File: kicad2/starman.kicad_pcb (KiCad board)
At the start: 2 copper layers, 160 x 150 mm, 156 parts, among them J1 Barrel_Jack, P1 USB_C_Plug_USB2.0, U1 ESP32-S2-MINI-1, U2 PCA9959, U3 PCA9959, U4 PCA9959, U5 PCA9959, U6 LF33_TO220, U7 LF50_TO220, U8 PCA9959, U9 PCA9959

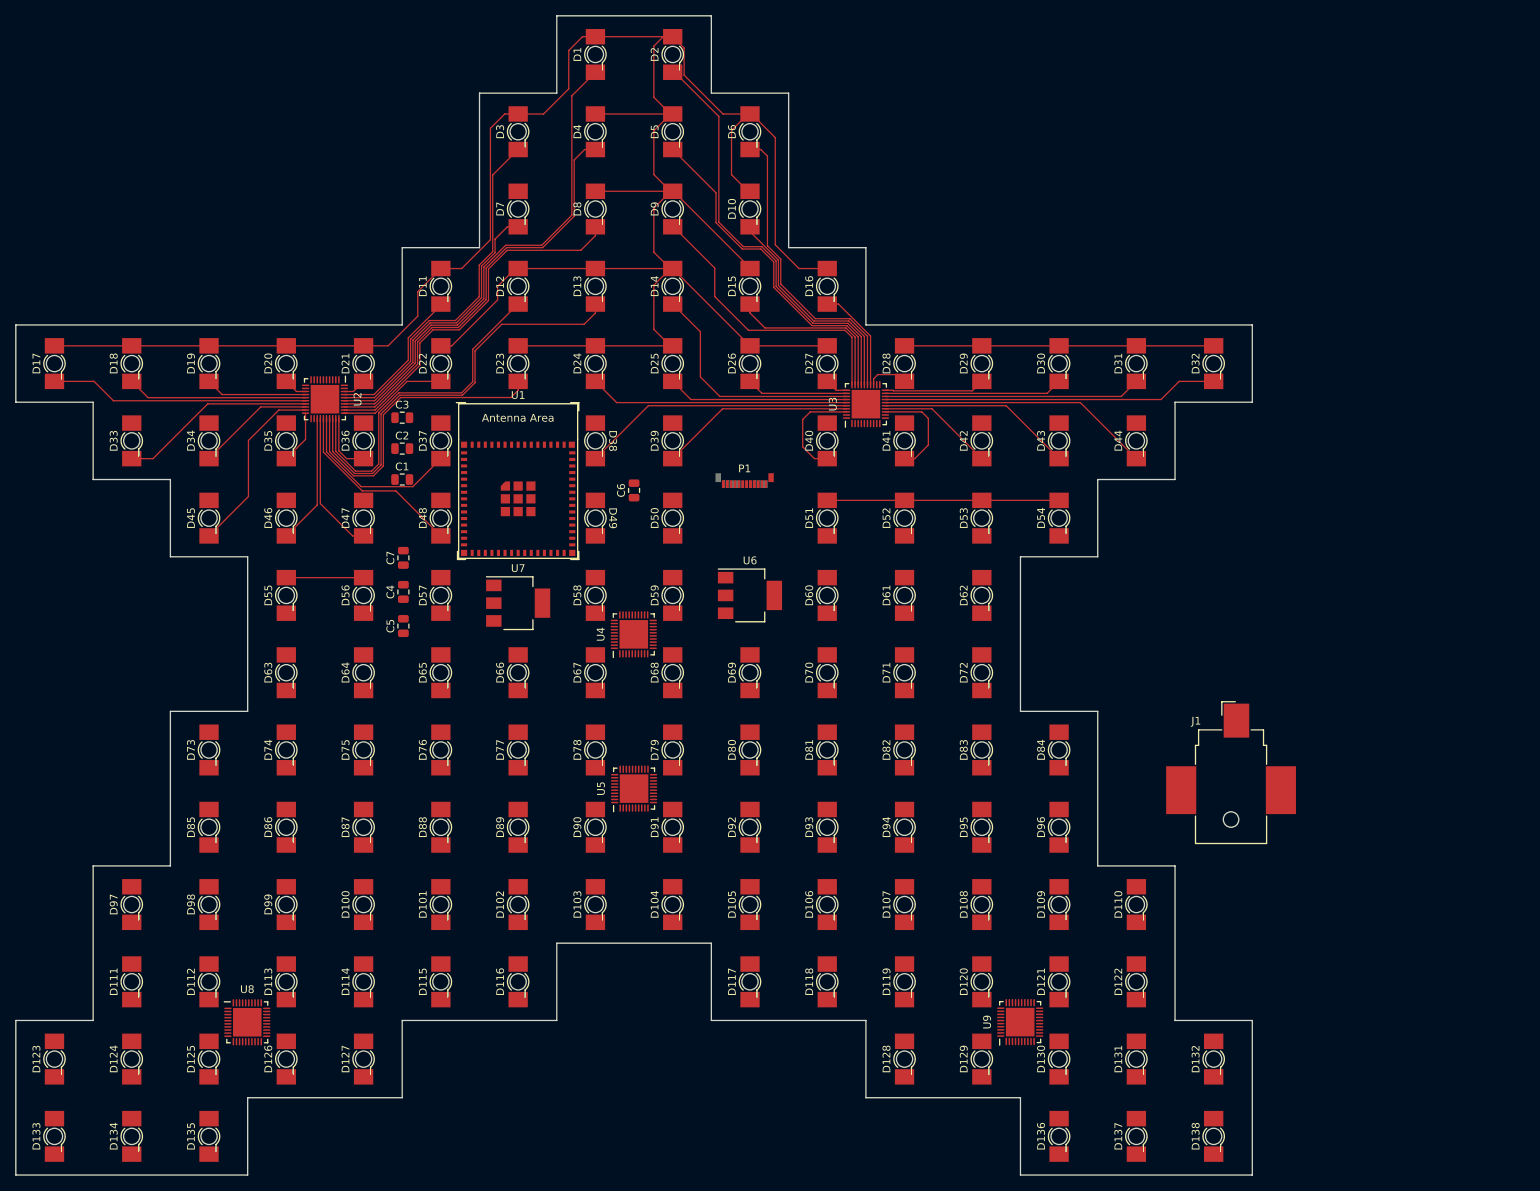
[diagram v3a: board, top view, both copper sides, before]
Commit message: Completed tracks to and from LED drivers
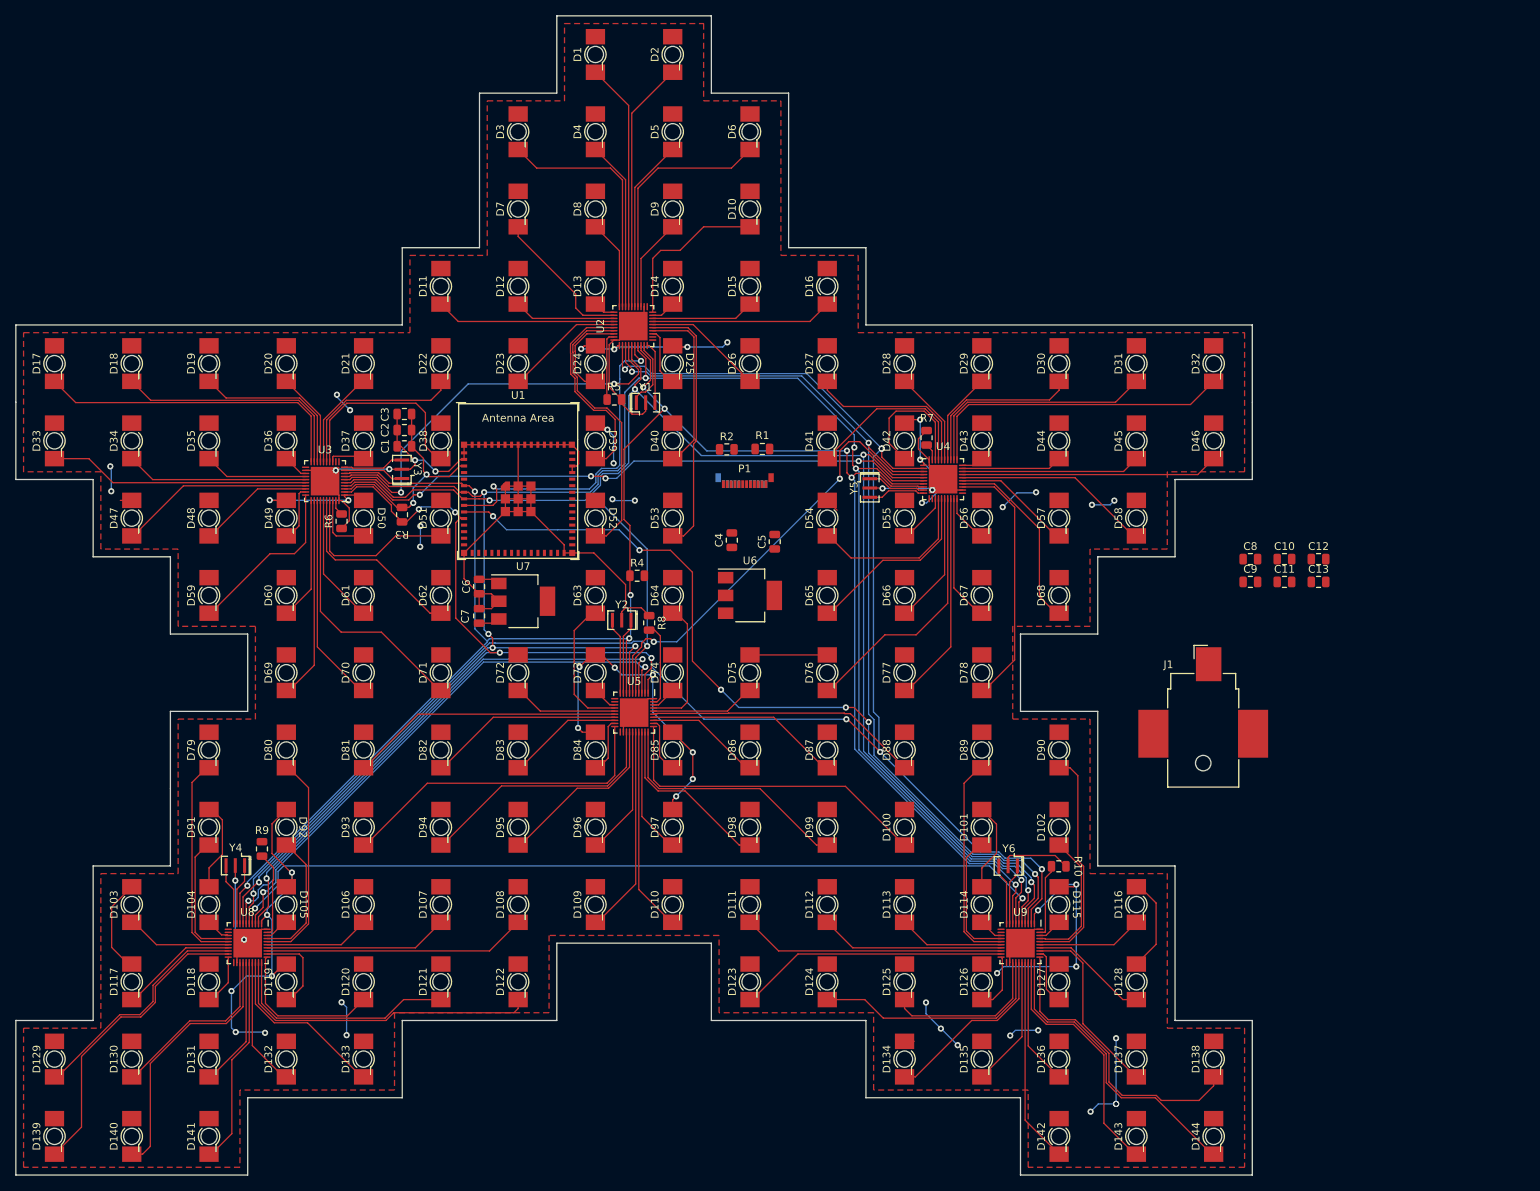
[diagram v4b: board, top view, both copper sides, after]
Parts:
- added C10: C, Capacitor_SMD:C_0805_2012Metric, F.Cu at (194.2, 100.3)
- added C11: C, Capacitor_SMD:C_0805_2012Metric, F.Cu at (194.2, 103.2)
- added C12: C, Capacitor_SMD:C_0805_2012Metric, F.Cu at (198.6, 100.3)
- added C13: C, Capacitor_SMD:C_0805_2012Metric, F.Cu at (198.6, 103.2)
- added C8: C, Capacitor_SMD:C_0805_2012Metric, F.Cu at (189.8, 100.3)
- added C9: C, Capacitor_SMD:C_0805_2012Metric, F.Cu at (189.8, 103.2)
- added D139: LED, LED_SMD:LED_Osram_Lx_P47F_D2mm_ReverseMount, F.Cu at (35.0, 175.0)
- added D140: LED, LED_SMD:LED_Osram_Lx_P47F_D2mm_ReverseMount, F.Cu at (45.0, 175.0)
- added D141: LED, LED_SMD:LED_Osram_Lx_P47F_D2mm_ReverseMount, F.Cu at (55.0, 175.0)
- added D142: LED, LED_SMD:LED_Osram_Lx_P47F_D2mm_ReverseMount, F.Cu at (165.0, 175.0)
- added D143: LED, LED_SMD:LED_Osram_Lx_P47F_D2mm_ReverseMount, F.Cu at (175.0, 175.0)
- added D144: LED, LED_SMD:LED_Osram_Lx_P47F_D2mm_ReverseMount, F.Cu at (185.0, 175.0)
- added R1: 5.1k, Resistor_SMD:R_0805_2012Metric, F.Cu at (126.6, 86.0)
- added R10: 3k, Resistor_SMD:R_0805_2012Metric, F.Cu at (164.9, 140.1)
- added R2: 5.1k, Resistor_SMD:R_0805_2012Metric, F.Cu at (122.0, 86.1)
- added R3: 10k, Resistor_SMD:R_0805_2012Metric, F.Cu at (80.0, 94.5)
- added R4: 10k, Resistor_SMD:R_0805_2012Metric, F.Cu at (110.4, 102.5)
- added R5: 3k, Resistor_SMD:R_0805_2012Metric, F.Cu at (107.5, 79.7)
- added R6: 3k, Resistor_SMD:R_0805_2012Metric, F.Cu at (72.2, 95.4)
- added R7: 3k, Resistor_SMD:R_0805_2012Metric, F.Cu at (147.8, 84.6)
- added R8: 3k, Resistor_SMD:R_0805_2012Metric, F.Cu at (112.0, 108.5)
- added R9: 3k, Resistor_SMD:R_0805_2012Metric, F.Cu at (61.9, 137.8)
- added Y1: 20Mhz, Crystal:Resonator_SMD_muRata_CSTxExxV-3Pin_3.0x1.1mm, F.Cu at (111.5, 80.0)
- added Y2: 20Mhz, Crystal:Resonator_SMD_muRata_CSTxExxV-3Pin_3.0x1.1mm, F.Cu at (108.4, 108.2)
- added Y3: 20Mhz, Crystal:Resonator_SMD_muRata_CSTxExxV-3Pin_3.0x1.1mm, F.Cu at (80.0, 88.7)
- added Y4: 20Mhz, Crystal:Resonator_SMD_muRata_CSTxExxV-3Pin_3.0x1.1mm, F.Cu at (58.4, 139.9)
- added Y5: 20Mhz, Crystal:Resonator_SMD_muRata_CSTxExxV-3Pin_3.0x1.1mm, F.Cu at (140.5, 91.1)
- added Y6: 20Mhz, Crystal:Resonator_SMD_muRata_CSTxExxV-3Pin_3.0x1.1mm, F.Cu at (158.4, 140.0)
- moved D45 120.4 mm to (175.0, 85.0)
- moved D46 120.4 mm to (185.0, 85.0)
- moved D129 120.0 mm to (35.0, 165.0)
- moved D130 120.0 mm to (45.0, 165.0)
- moved D131 120.0 mm to (55.0, 165.0)
- moved D132 120.0 mm to (65.0, 165.0)
- moved D134 100.5 mm to (145.0, 165.0)
- moved D135 100.5 mm to (155.0, 165.0)
- moved D123 90.6 mm to (125.0, 155.0)
- moved D124 90.6 mm to (135.0, 155.0)
- moved D125 90.6 mm to (145.0, 155.0)
- moved D126 90.6 mm to (155.0, 155.0)
- moved D127 90.6 mm to (165.0, 155.0)
- moved D111 80.6 mm to (125.0, 145.0)
- moved D112 80.6 mm to (135.0, 145.0)
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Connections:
- D1 pad 2: (no net) -> +5V
- D10 pad 2: (no net) -> +5V
- D100 pad 2: (no net) -> +5V
- D101 pad 2: (no net) -> +5V
- D102 pad 2: (no net) -> +5V
- D103 pad 2: (no net) -> +5V
- D104 pad 2: (no net) -> +5V
- D105 pad 2: (no net) -> +5V
- D106 pad 2: (no net) -> +5V
- D107 pad 2: (no net) -> +5V
- D108 pad 2: (no net) -> +5V
- D109 pad 2: (no net) -> +5V
- D11 pad 2: (no net) -> +5V
- D110 pad 2: (no net) -> +5V
- D111 pad 2: (no net) -> +5V
- D112 pad 2: (no net) -> +5V
- D113 pad 2: (no net) -> +5V
- D114 pad 2: (no net) -> +5V
- D115 pad 2: (no net) -> +5V
- D116 pad 2: (no net) -> +5V
- D117 pad 2: (no net) -> +5V
- D118 pad 2: (no net) -> +5V
- D119 pad 2: (no net) -> +5V
- D12 pad 2: (no net) -> +5V
- D120 pad 2: (no net) -> +5V
- D121 pad 2: (no net) -> +5V
- D122 pad 2: (no net) -> +5V
- D123 pad 2: (no net) -> +5V
- D124 pad 2: (no net) -> +5V
- D125 pad 2: (no net) -> +5V
- D126 pad 2: (no net) -> +5V
- D127 pad 2: (no net) -> +5V
- D128 pad 2: (no net) -> +5V
- D129 pad 2: (no net) -> +5V
- D13 pad 2: (no net) -> +5V
- D130 pad 2: (no net) -> +5V
- D131 pad 2: (no net) -> +5V
- D132 pad 2: (no net) -> +5V
- D133 pad 2: (no net) -> +5V
- D134 pad 2: (no net) -> +5V
- D135 pad 2: (no net) -> +5V
- D136 pad 2: (no net) -> +5V
- D137 pad 2: (no net) -> +5V
- D138 pad 2: (no net) -> +5V
- D14 pad 2: (no net) -> +5V
- D15 pad 2: (no net) -> +5V
- D16 pad 2: (no net) -> +5V
- D17 pad 2: (no net) -> +5V
- D18 pad 2: (no net) -> +5V
- D19 pad 2: (no net) -> +5V
- D2 pad 2: (no net) -> +5V
- D20 pad 2: (no net) -> +5V
- D21 pad 2: (no net) -> +5V
- D22 pad 2: (no net) -> +5V
- D23 pad 2: (no net) -> +5V
- D24 pad 2: (no net) -> +5V
- D25 pad 2: (no net) -> +5V
- D26 pad 2: (no net) -> +5V
- D27 pad 2: (no net) -> +5V
- D28 pad 2: (no net) -> +5V
- D29 pad 2: (no net) -> +5V
- D3 pad 2: (no net) -> +5V
- D30 pad 2: (no net) -> +5V
- D31 pad 2: (no net) -> +5V
- D32 pad 2: (no net) -> +5V
- D33 pad 2: (no net) -> +5V
- D34 pad 2: (no net) -> +5V
- D35 pad 2: (no net) -> +5V
- D36 pad 2: (no net) -> +5V
- D37 pad 2: (no net) -> +5V
- D38 pad 2: (no net) -> +5V
- D39 pad 2: (no net) -> +5V
- D4 pad 2: (no net) -> +5V
- D40 pad 2: (no net) -> +5V
- D41 pad 2: (no net) -> +5V
- D42 pad 2: (no net) -> +5V
- D43 pad 2: (no net) -> +5V
- D44 pad 2: (no net) -> +5V
- D45 pad 2: (no net) -> +5V
- D46 pad 2: (no net) -> +5V
- D47 pad 2: (no net) -> +5V
- D48 pad 2: (no net) -> +5V
- D49 pad 2: (no net) -> +5V
- D5 pad 2: (no net) -> +5V
- D50 pad 2: (no net) -> +5V
- D51 pad 2: (no net) -> +5V
- D52 pad 2: (no net) -> +5V
- D53 pad 2: (no net) -> +5V
- D54 pad 2: (no net) -> +5V
- D55 pad 2: (no net) -> +5V
- D56 pad 2: (no net) -> +5V
- D57 pad 2: (no net) -> +5V
- D58 pad 2: (no net) -> +5V
- D59 pad 2: (no net) -> +5V
- D6 pad 2: (no net) -> +5V
- D60 pad 2: (no net) -> +5V
- D61 pad 2: (no net) -> +5V
- D62 pad 2: (no net) -> +5V
- D63 pad 2: (no net) -> +5V
- D64 pad 2: (no net) -> +5V
- D65 pad 2: (no net) -> +5V
- D66 pad 2: (no net) -> +5V
- D67 pad 2: (no net) -> +5V
- D68 pad 2: (no net) -> +5V
- D69 pad 2: (no net) -> +5V
- D7 pad 2: (no net) -> +5V
- D70 pad 2: (no net) -> +5V
- D71 pad 2: (no net) -> +5V
- D72 pad 2: (no net) -> +5V
- D73 pad 1: (no net) -> Net-(D73-Pad1)
- D73 pad 2: (no net) -> +5V
- D74 pad 2: (no net) -> +5V
- D75 pad 2: (no net) -> +5V
- D76 pad 2: (no net) -> +5V
- D77 pad 2: (no net) -> +5V
- D78 pad 2: (no net) -> +5V
- D79 pad 2: (no net) -> +5V
- D8 pad 2: (no net) -> +5V
- D80 pad 2: (no net) -> +5V
- D81 pad 2: (no net) -> +5V
- D82 pad 2: (no net) -> +5V
- D83 pad 2: (no net) -> +5V
- D84 pad 2: (no net) -> +5V
- D85 pad 2: (no net) -> +5V
- D86 pad 2: (no net) -> +5V
- D87 pad 2: (no net) -> +5V
- D88 pad 2: (no net) -> +5V
- D89 pad 2: (no net) -> +5V
- D9 pad 2: (no net) -> +5V
- D90 pad 2: (no net) -> +5V
- D91 pad 2: (no net) -> +5V
- D92 pad 2: (no net) -> +5V
- D93 pad 2: (no net) -> +5V
- D94 pad 2: (no net) -> +5V
- D95 pad 2: (no net) -> +5V
- D96 pad 2: (no net) -> +5V
- D97 pad 2: (no net) -> +5V
- D98 pad 2: (no net) -> +5V
- D99 pad 2: (no net) -> +5V
- P1 pad A5: (no net) -> Net-(P1-PadA5)
- P1 pad B5: (no net) -> Net-(P1-PadB5)
- U1 pad 10: (no net) -> /MISO
- U1 pad 11: (no net) -> /RESET
- U1 pad 6: (no net) -> /OE
- U1 pad 7: (no net) -> /CS
- U1 pad 8: (no net) -> /SCLK
- U1 pad 9: (no net) -> /MOSI
- U2 pad 1: (no net) -> +5V
- U2 pad 10: (no net) -> Net-(U2-Pad10)
- U2 pad 13: Net-(D20-Pad1) -> Net-(D25-Pad1)
- U2 pad 14: Net-(D19-Pad1) -> Net-(D40-Pad1)
- U2 pad 15: Net-(D18-Pad1) -> Net-(D53-Pad1)
- U2 pad 16: Net-(D17-Pad1) -> Net-(D26-Pad1)
- U2 pad 17: Net-(D33-Pad1) -> Net-(D16-Pad1)
- U2 pad 18: Net-(D34-Pad1) -> Net-(D15-Pad1)
- U2 pad 19: Net-(D45-Pad1) -> Net-(D14-Pad1)
- U2 pad 2: (no net) -> /RESET
- U2 pad 20: Net-(D35-Pad1) -> Net-(D10-Pad1)
- U2 pad 22: (no net) -> GND
- U2 pad 23: Net-(D46-Pad1) -> Net-(D9-Pad1)
- U2 pad 24: Net-(D47-Pad1) -> Net-(D6-Pad1)
- U2 pad 25: Net-(D48-Pad1) -> Net-(D5-Pad1)
- U2 pad 26: Net-(D37-Pad1) -> Net-(D2-Pad1)
- U2 pad 27: Net-(D23-Pad1) -> Net-(D1-Pad1)
- U2 pad 28: Net-(D13-Pad1) -> Net-(D4-Pad1)
- U2 pad 29: Net-(D12-Pad1) -> Net-(D3-Pad1)
- U2 pad 3: (no net) -> +3V3
- U2 pad 30: Net-(D36-Pad1) -> Net-(D8-Pad1)
- U2 pad 31: Net-(D22-Pad1) -> Net-(D13-Pad1)
- U2 pad 32: Net-(D8-Pad1) -> Net-(D7-Pad1)
- U2 pad 33: Net-(D4-Pad1) -> Net-(D12-Pad1)
- U2 pad 34: Net-(D1-Pad1) -> Net-(D11-Pad1)
- U2 pad 35: Net-(D7-Pad1) -> Net-(D23-Pad1)
- U2 pad 36: Net-(D3-Pad1) -> Net-(D39-Pad1)
- U2 pad 37: Net-(D11-Pad1) -> Net-(D52-Pad1)
- U2 pad 38: Net-(D21-Pad1) -> Net-(D24-Pad1)
- U2 pad 39: (no net) -> Net-(R5-Pad2)
- U2 pad 4: (no net) -> Net-(U2-Pad4)
- U2 pad 40: (no net) -> GND
- U2 pad 41: Net-(U2-Pad41) -> GND
- U2 pad 5: (no net) -> /SCLK
- U2 pad 6: (no net) -> /MOSI
- U2 pad 7: (no net) -> /CS
- U2 pad 8: (no net) -> /OE
- U2 pad 9: (no net) -> Net-(U2-Pad9)
- U3 pad 1: (no net) -> +5V
- U3 pad 10: (no net) -> Net-(U3-Pad10)
- U3 pad 13: Net-(D41-Pad1) -> Net-(D37-Pad1)
- U3 pad 14: Net-(D42-Pad1) -> Net-(D38-Pad1)
- U3 pad 15: Net-(D43-Pad1) -> Net-(D22-Pad1)
- U3 pad 16: Net-(D44-Pad1) -> Net-(D21-Pad1)
- U3 pad 17: Net-(D32-Pad1) -> Net-(D20-Pad1)
- U3 pad 18: Net-(D31-Pad1) -> Net-(D19-Pad1)
- U3 pad 19: Net-(D30-Pad1) -> Net-(D18-Pad1)
- U3 pad 2: (no net) -> /RESET
- U3 pad 20: Net-(D29-Pad1) -> Net-(D17-Pad1)
- U3 pad 22: (no net) -> GND
- U3 pad 23: Net-(D28-Pad1) -> Net-(D36-Pad1)
- U3 pad 24: Net-(D16-Pad1) -> Net-(D35-Pad1)
- U3 pad 25: Net-(D6-Pad1) -> Net-(D34-Pad1)
- U3 pad 26: Net-(D10-Pad1) -> Net-(D33-Pad1)
- U3 pad 27: Net-(D2-Pad1) -> Net-(D47-Pad1)
- U3 pad 28: Net-(D5-Pad1) -> Net-(D48-Pad1)
- U3 pad 29: Net-(D15-Pad1) -> Net-(D49-Pad1)
- U3 pad 3: (no net) -> +3V3
- U3 pad 30: Net-(D9-Pad1) -> Net-(D59-Pad1)
- U3 pad 31: Net-(D27-Pad1) -> Net-(D60-Pad1)
- U3 pad 32: Net-(D26-Pad1) -> Net-(D69-Pad1)
- U3 pad 33: Net-(D14-Pad1) -> Net-(D70-Pad1)
- U3 pad 34: Net-(D25-Pad1) -> Net-(D71-Pad1)
- U3 pad 35: Net-(D24-Pad1) -> Net-(D61-Pad1)
- U3 pad 36: Net-(D38-Pad1) -> Net-(D62-Pad1)
- U3 pad 37: Net-(D39-Pad1) -> Net-(D51-Pad1)
- U3 pad 38: Net-(D40-Pad1) -> Net-(D50-Pad1)
- U3 pad 39: (no net) -> Net-(R6-Pad2)
- U3 pad 4: (no net) -> Net-(U3-Pad4)
- U3 pad 40: (no net) -> GND
- U3 pad 41: Net-(U3-Pad41) -> GND
- U3 pad 5: (no net) -> /SCLK
- U3 pad 6: (no net) -> Net-(U2-Pad4)
- U3 pad 7: (no net) -> /CS
- U3 pad 8: (no net) -> /OE
- U3 pad 9: (no net) -> Net-(U3-Pad9)
- U4 pad 1: (no net) -> +5V
- U4 pad 10: (no net) -> Net-(U4-Pad10)
- U4 pad 13: Net-(D49-Pad1) -> Net-(D55-Pad1)
- U4 pad 14: Net-(D50-Pad1) -> Net-(D54-Pad1)
- U4 pad 15: Net-(D51-Pad1) -> Net-(D65-Pad1)
- U4 pad 16: Net-(D52-Pad1) -> Net-(D66-Pad1)
- U4 pad 17: Net-(D53-Pad1) -> Net-(D76-Pad1)
- U4 pad 18: Net-(D54-Pad1) -> Net-(D77-Pad1)
- U4 pad 19: Net-(D55-Pad1) -> Net-(D67-Pad1)
- U4 pad 2: (no net) -> /RESET
- U4 pad 22: (no net) -> GND
- U4 pad 23: Net-(D57-Pad1) -> Net-(D78-Pad1)
- U4 pad 24: Net-(D58-Pad1) -> Net-(D68-Pad1)
- U4 pad 25: Net-(D59-Pad1) -> Net-(D57-Pad1)
- U4 pad 26: Net-(D60-Pad1) -> Net-(D58-Pad1)
- U4 pad 27: Net-(D61-Pad1) -> Net-(D46-Pad1)
- U4 pad 28: Net-(D62-Pad1) -> Net-(D45-Pad1)
- U4 pad 29: Net-(D63-Pad1) -> Net-(D44-Pad1)
- U4 pad 3: (no net) -> +3V3
- U4 pad 30: Net-(D64-Pad1) -> Net-(D43-Pad1)
- U4 pad 31: Net-(D65-Pad1) -> Net-(D32-Pad1)
- U4 pad 32: Net-(D66-Pad1) -> Net-(D31-Pad1)
- U4 pad 33: Net-(D67-Pad1) -> Net-(D30-Pad1)
- U4 pad 34: Net-(D68-Pad1) -> Net-(D29-Pad1)
- U4 pad 35: Net-(D69-Pad1) -> Net-(D28-Pad1)
- U4 pad 36: Net-(D70-Pad1) -> Net-(D27-Pad1)
- U4 pad 37: Net-(D71-Pad1) -> Net-(D41-Pad1)
- U4 pad 38: Net-(D72-Pad1) -> Net-(D42-Pad1)
- U4 pad 39: (no net) -> Net-(R7-Pad2)
- U4 pad 4: (no net) -> Net-(U4-Pad4)
- U4 pad 40: (no net) -> GND
- U4 pad 41: Net-(U4-Pad41) -> GND
- U4 pad 5: (no net) -> /SCLK
- U4 pad 6: (no net) -> Net-(U3-Pad4)
- U4 pad 7: (no net) -> /CS
- U4 pad 8: (no net) -> /OE
- U4 pad 9: (no net) -> Net-(U4-Pad9)
- U5 pad 1: (no net) -> +5V
- U5 pad 10: (no net) -> Net-(U5-Pad10)
- U5 pad 13: (no net) -> Net-(D73-Pad1)
- U5 pad 14: Net-(D96-Pad1) -> Net-(D63-Pad1)
- U5 pad 15: Net-(D95-Pad1) -> Net-(D72-Pad1)
- U5 pad 16: Net-(D94-Pad1) -> Net-(D81-Pad1)
- U5 pad 17: Net-(D93-Pad1) -> Net-(D82-Pad1)
- U5 pad 18: Net-(D92-Pad1) -> Net-(D83-Pad1)
- U5 pad 19: Net-(D91-Pad1) -> Net-(D84-Pad1)
- U5 pad 2: (no net) -> /RESET
- U5 pad 20: Net-(D90-Pad1) -> Net-(D93-Pad1)
- U5 pad 22: (no net) -> GND
- U5 pad 23: Net-(D89-Pad1) -> Net-(D94-Pad1)
- U5 pad 24: Net-(D88-Pad1) -> Net-(D95-Pad1)
- U5 pad 25: Net-(D87-Pad1) -> Net-(D96-Pad1)
- U5 pad 26: Net-(D86-Pad1) -> Net-(D109-Pad1)
- U5 pad 27: Net-(D85-Pad1) -> Net-(D110-Pad1)
- U5 pad 28: Net-(D84-Pad1) -> Net-(D97-Pad1)
- U5 pad 29: Net-(D83-Pad1) -> Net-(D98-Pad1)
- U5 pad 3: (no net) -> +3V3
- U5 pad 30: Net-(D82-Pad1) -> Net-(D99-Pad1)
- U5 pad 31: Net-(D81-Pad1) -> Net-(D100-Pad1)
- U5 pad 32: Net-(D80-Pad1) -> Net-(D85-Pad1)
- U5 pad 33: Net-(D79-Pad1) -> Net-(D86-Pad1)
- U5 pad 34: Net-(D78-Pad1) -> Net-(D87-Pad1)
- U5 pad 35: Net-(D77-Pad1) -> Net-(D88-Pad1)
- U5 pad 36: Net-(D76-Pad1) -> Net-(D75-Pad1)
- U5 pad 37: Net-(D75-Pad1) -> Net-(D64-Pad1)
- U5 pad 39: (no net) -> Net-(R8-Pad2)
- U5 pad 4: (no net) -> Net-(U5-Pad4)
- U5 pad 40: (no net) -> GND
- U5 pad 41: Net-(U5-Pad41) -> GND
- U5 pad 5: (no net) -> /SCLK
- U5 pad 6: (no net) -> Net-(U4-Pad4)
- U5 pad 7: (no net) -> /CS
- U5 pad 8: (no net) -> /OE
- U5 pad 9: (no net) -> Net-(U5-Pad9)
- U8 pad 1: (no net) -> +5V
- U8 pad 10: (no net) -> Net-(U8-Pad10)
- U8 pad 13: Net-(D97-Pad1) -> Net-(D104-Pad1)
- U8 pad 14: Net-(D98-Pad1) -> Net-(D91-Pad1)
- U8 pad 15: Net-(D99-Pad1) -> Net-(D79-Pad1)
- U8 pad 16: Net-(D100-Pad1) -> Net-(D103-Pad1)
- U8 pad 17: Net-(D101-Pad1) -> Net-(D117-Pad1)
- U8 pad 18: Net-(D102-Pad1) -> Net-(D129-Pad1)
- U8 pad 19: Net-(D103-Pad1) -> Net-(D139-Pad1)
- U8 pad 2: (no net) -> /RESET
- U8 pad 20: Net-(D111-Pad1) -> Net-(D118-Pad1)
- U8 pad 22: (no net) -> GND
- U8 pad 23: Net-(D112-Pad1) -> Net-(D130-Pad1)
- U8 pad 24: Net-(D113-Pad1) -> Net-(D140-Pad1)
- U8 pad 25: Net-(D114-Pad1) -> Net-(D131-Pad1)
- U8 pad 26: Net-(D115-Pad1) -> Net-(D141-Pad1)
- U8 pad 27: Net-(D116-Pad1) -> Net-(D132-Pad1)
- U8 pad 28: Net-(D123-Pad1) -> Net-(D133-Pad1)
- U8 pad 29: Net-(D124-Pad1) -> Net-(D122-Pad1)
- U8 pad 3: (no net) -> +3V3
- U8 pad 30: Net-(D125-Pad1) -> Net-(D121-Pad1)
- U8 pad 31: Net-(D126-Pad1) -> Net-(D120-Pad1)
- U8 pad 32: Net-(D127-Pad1) -> Net-(D119-Pad1)
- U8 pad 33: Net-(D133-Pad1) -> Net-(D108-Pad1)
- U8 pad 34: Net-(D134-Pad1) -> Net-(D107-Pad1)
- U8 pad 35: Net-(D135-Pad1) -> Net-(D106-Pad1)
- U8 pad 36: (no net) -> Net-(D80-Pad1)
- U8 pad 37: (no net) -> Net-(D92-Pad1)
- U8 pad 38: (no net) -> Net-(D105-Pad1)
- U8 pad 39: (no net) -> Net-(R9-Pad2)
- U8 pad 4: (no net) -> Net-(U8-Pad4)
- U8 pad 40: (no net) -> GND
- U8 pad 41: Net-(U8-Pad41) -> GND
- U8 pad 5: (no net) -> /SCLK
- U8 pad 6: (no net) -> Net-(U5-Pad4)
- U8 pad 7: (no net) -> /CS
- U8 pad 8: (no net) -> /OE
- U8 pad 9: (no net) -> Net-(U8-Pad9)
- U9 pad 1: (no net) -> +5V
- U9 pad 10: (no net) -> Net-(U9-Pad10)
- U9 pad 13: Net-(D104-Pad1) -> Net-(D114-Pad1)
- U9 pad 14: Net-(D105-Pad1) -> Net-(D101-Pad1)
- U9 pad 15: Net-(D106-Pad1) -> Net-(D89-Pad1)
- U9 pad 16: Net-(D107-Pad1) -> Net-(D113-Pad1)
- U9 pad 17: Net-(D108-Pad1) -> Net-(D112-Pad1)
- U9 pad 18: Net-(D109-Pad1) -> Net-(D111-Pad1)
- U9 pad 19: Net-(D110-Pad1) -> Net-(D123-Pad1)
- U9 pad 2: (no net) -> /RESET
- U9 pad 20: Net-(D117-Pad1) -> Net-(D126-Pad1)
- U9 pad 22: (no net) -> GND
- U9 pad 23: Net-(D118-Pad1) -> Net-(D125-Pad1)
- U9 pad 24: Net-(D119-Pad1) -> Net-(D124-Pad1)
- U9 pad 25: Net-(D120-Pad1) -> Net-(D134-Pad1)
- U9 pad 26: Net-(D121-Pad1) -> Net-(D135-Pad1)
- U9 pad 27: Net-(D122-Pad1) -> Net-(D142-Pad1)
- U9 pad 28: Net-(D128-Pad1) -> Net-(D136-Pad1)
- U9 pad 29: Net-(D129-Pad1) -> Net-(D143-Pad1)
- U9 pad 3: (no net) -> +3V3
- U9 pad 30: Net-(D130-Pad1) -> Net-(D144-Pad1)
- U9 pad 31: Net-(D131-Pad1) -> Net-(D138-Pad1)
- U9 pad 32: Net-(D132-Pad1) -> Net-(D127-Pad1)
- U9 pad 33: Net-(D136-Pad1) -> Net-(D137-Pad1)
- U9 pad 34: Net-(D137-Pad1) -> Net-(D128-Pad1)
- U9 pad 35: Net-(D138-Pad1) -> Net-(D116-Pad1)
- U9 pad 36: (no net) -> Net-(D90-Pad1)
- U9 pad 37: (no net) -> Net-(D102-Pad1)
- U9 pad 38: (no net) -> Net-(D115-Pad1)
- U9 pad 39: (no net) -> Net-(R10-Pad2)
- U9 pad 4: (no net) -> /MISO
- U9 pad 40: (no net) -> GND
- U9 pad 41: Net-(U9-Pad41) -> GND
- U9 pad 5: (no net) -> /SCLK
- U9 pad 6: (no net) -> Net-(U8-Pad4)
- U9 pad 7: (no net) -> /CS
- U9 pad 8: (no net) -> /OE
- U9 pad 9: (no net) -> Net-(U9-Pad9)
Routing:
- net (no net): track 408.1 -> 0.00 mm
- net +5V: track 0.00 -> 303.2 mm, vias 0 -> 51
- net GND: track 0.00 -> 275.7 mm, vias 0 -> 8
- net /RESET: track 0.00 -> 273.1 mm, vias 0 -> 11
- net /SCLK: track 0.00 -> 272.0 mm, vias 0 -> 6
- net /CS: track 0.00 -> 267.2 mm, vias 0 -> 9
- net /OE: track 0.00 -> 264.7 mm, vias 0 -> 9
- net +3V3: track 0.00 -> 222.5 mm, vias 0 -> 7
- net Net-(U8-Pad4): track 0.00 -> 110.0 mm, vias 0 -> 2
- net /MISO: track 0.00 -> 108.7 mm, vias 0 -> 6
- net Net-(U3-Pad4): track 0.00 -> 79.5 mm, vias 0 -> 4
- net Net-(U5-Pad4): track 0.00 -> 73.0 mm, vias 0 -> 2
- net Net-(U4-Pad4): track 0.00 -> 58.5 mm, vias 0 -> 2
- net Net-(U2-Pad4): track 0.00 -> 52.7 mm, vias 0 -> 2
- net Net-(D13-Pad1): track 55.5 -> 2.82 mm
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- added copper zone on F.Cu, net +5V
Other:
- outline, holes or cut-outs redrawn

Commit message: Added mounting headers -- will move barrel jack and usb to daughter board
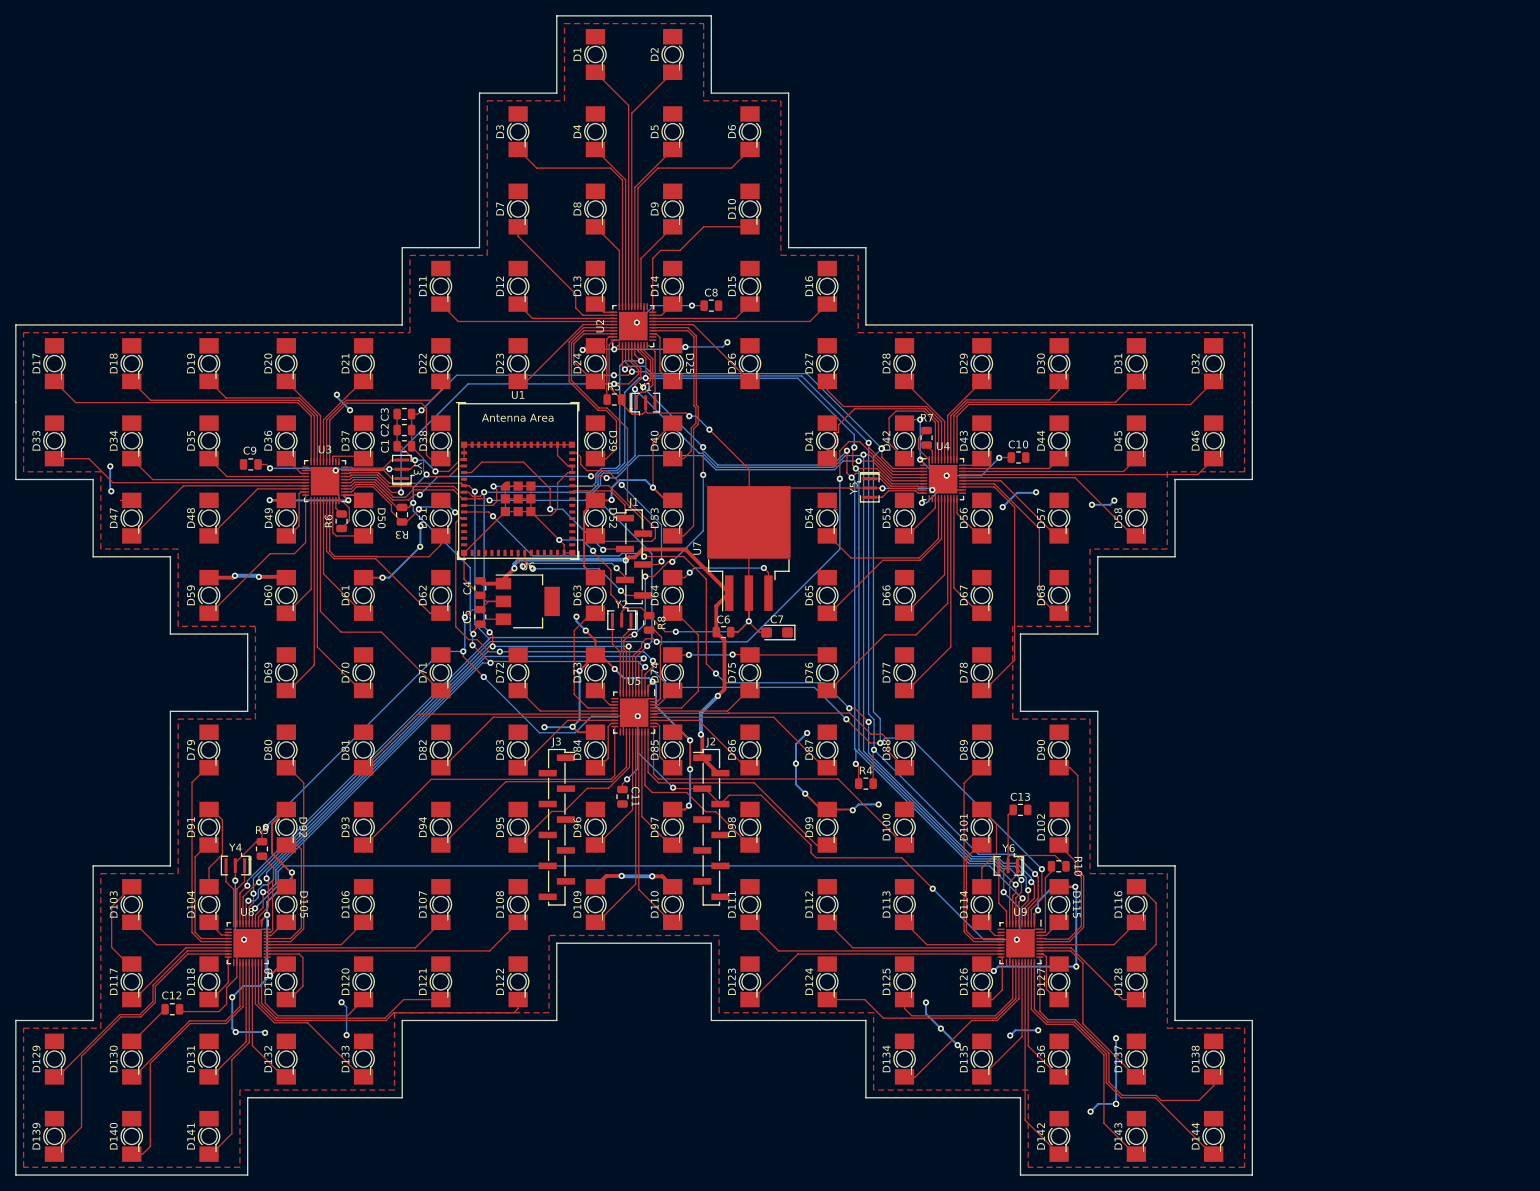
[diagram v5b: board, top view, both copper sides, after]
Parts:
- removed the C11 at (194.2, 103.2)
- removed P1: USB_C_Plug_USB2.0, Connector_USB:USB_C_Plug_Molex_105444
- removed R1, R2: 5.1k, Resistor_SMD:R_0805_2012Metric
- added C10: C, Capacitor_SMD:C_0805_2012Metric, F.Cu at (159.8, 87.2)
- added J2: Conn_01x10, Connector_PinHeader_2.00mm:PinHeader_1x10_P2.00mm_Vertical_SMD_Pin1Left, F.Cu at (120.0, 135.0)
- added J3: Conn_01x10, Connector_PinHeader_2.00mm:PinHeader_1x10_P2.00mm_Vertical_SMD_Pin1Right, F.Cu at (100.0, 135.0)
- C6: value C -> 0.1uF
- C7: value C -> 10uF; footprint Capacitor_SMD:C_0805_2012Metric -> Capacitor_Tantalum_SMD:CP_EIA-3216-10_Kemet-I
- J1: value Barrel_Jack -> Conn_01x10; footprint Connector_BarrelJack:BarrelJack_CUI_PJ-036AH-SMT_Horizontal -> Connector_PinHeader_2.00mm:PinHeader_1x06_P2.00mm_Vertical_SMD_Pin1Left
- U7: value LF50_TO220 -> MIC29310-5.0WU; footprint Package_TO_SOT_SMD:SOT-223 -> Package_TO_SOT_SMD:TO-263-3_TabPin2
- moved C12 159.3 mm to (50.2, 158.6), turned to 180 degrees
- moved C9 134.3 mm to (60.4, 88.0), turned to 180 degrees
- moved C11 85.9 mm to (108.5, 131.1), turned to 270 degrees
- moved C8 77.1 mm to (120.0, 67.5)
- moved J1 76.2 mm to (110.0, 100.0)
- moved C13 48.6 mm to (160.0, 132.8)
- moved R4 40.0 mm to (140.0, 129.3)
- moved C5 39.3 mm to (90.1, 107.8), turned to 270 degrees
- moved C7 38.6 mm to (128.5, 109.8), turned to 180 degrees
- moved C4 33.1 mm to (90.1, 104.0)
- moved C6 32.2 mm to (121.6, 109.8), turned to 180 degrees
- moved U7 30.0 mm to (124.8, 98.9), turned to 90 degrees
- moved U6 28.8 mm to (96.2, 105.8)
- renumbered C9 to C11, C10 to C9
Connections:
- C7 pad 1: GND -> +5V
- C7 pad 2: +5V -> GND
- J1 pad 1: Net-(C4-Pad2) -> /TXD
- J1 pad 2: GND -> /RXD
- J1 pad 3: (no net) -> /BOOT
- U1 pad 39: (no net) -> /TXD
- U1 pad 4: (no net) -> /BOOT
- U1 pad 40: (no net) -> /RXD
- U1 pad 45: (no net) -> /ESP_RESET
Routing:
- net GND: track 275.7 -> 572.0 mm, vias 8 -> 29
- net +5V: track 303.2 -> 413.7 mm, vias 51 -> 66
- net +3V3: track 222.5 -> 287.4 mm, vias 7 -> 13
- net Net-(C4-Pad2): track 2.77 -> 64.2 mm, vias 0 -> 4
- net /BOOT: track 0.00 -> 27.7 mm, vias 0 -> 2
- net /ESP_RESET: track 0.00 -> 23.3 mm, vias 0 -> 2
- net /USBDP: track 0.00 -> 18.2 mm, vias 0 -> 2
- net /USBDM: track 0.00 -> 16.5 mm, vias 0 -> 2
- net /RXD: track 0.00 -> 12.8 mm
- net /TXD: track 0.00 -> 9.35 mm
- net Net-(D52-Pad1): track 36.6 -> 44.7 mm
- net /OE: track 264.7 -> 270.1 mm, vias 9 -> 12
- net Net-(U4-Pad4): track 58.5 -> 63.8 mm
- net Net-(D41-Pad1): track 22.7 -> 25.5 mm
- net /SCLK: track 272.0 -> 273.7 mm
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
